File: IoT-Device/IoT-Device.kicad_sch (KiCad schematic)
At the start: 49 parts, among them J1 USB-C, J2 Conn_01x02, J3 SWD, SW1 RESET, SW2 BOOT_MODE, U1 BD33GA5WEFJ, U2 STM32U585VI, U3 BQ24074RGT, U4 ESP32-C3-WROOM-02

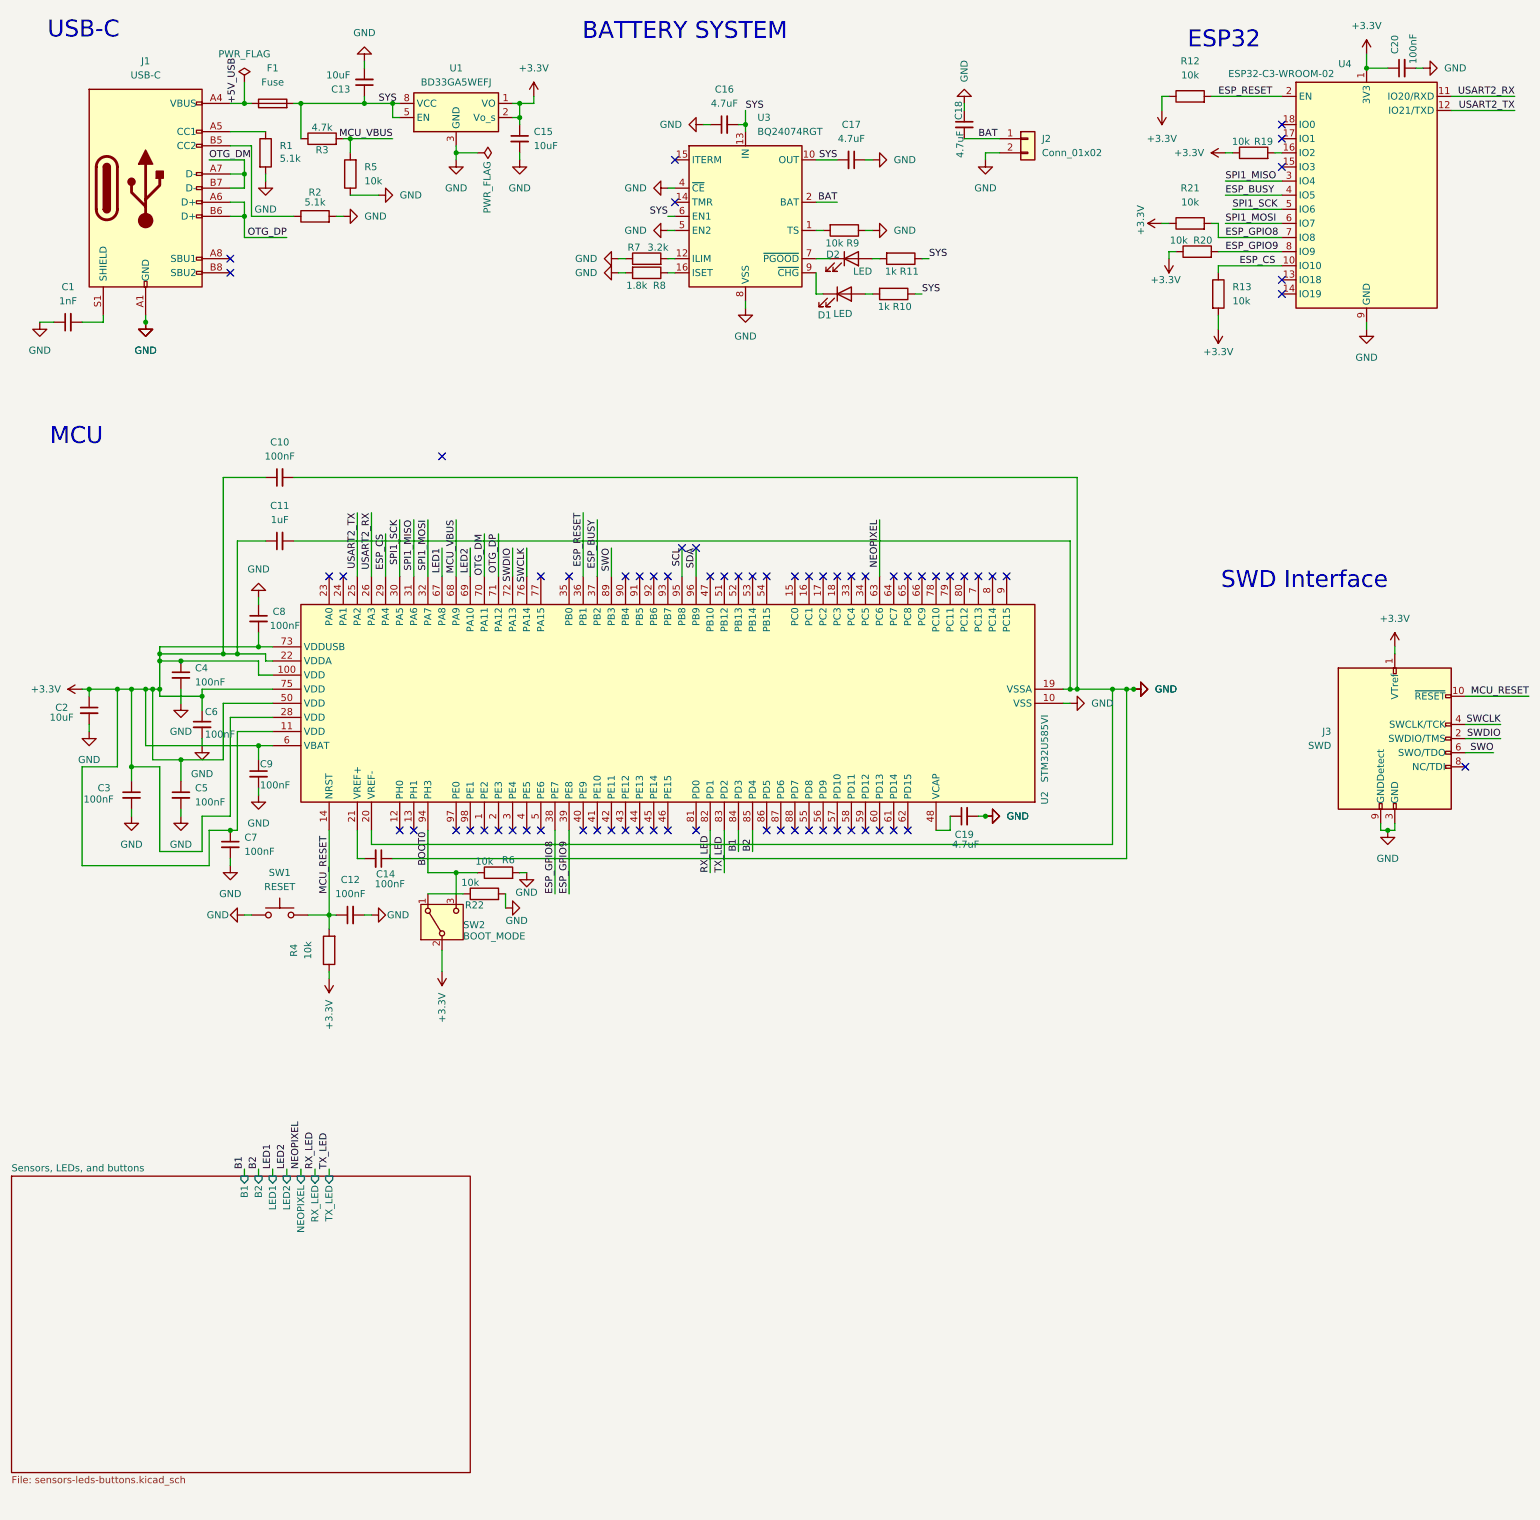
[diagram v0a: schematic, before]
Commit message: connect USB-C port's CC1 and CC2 to STM32's CC1 and CC2 pins
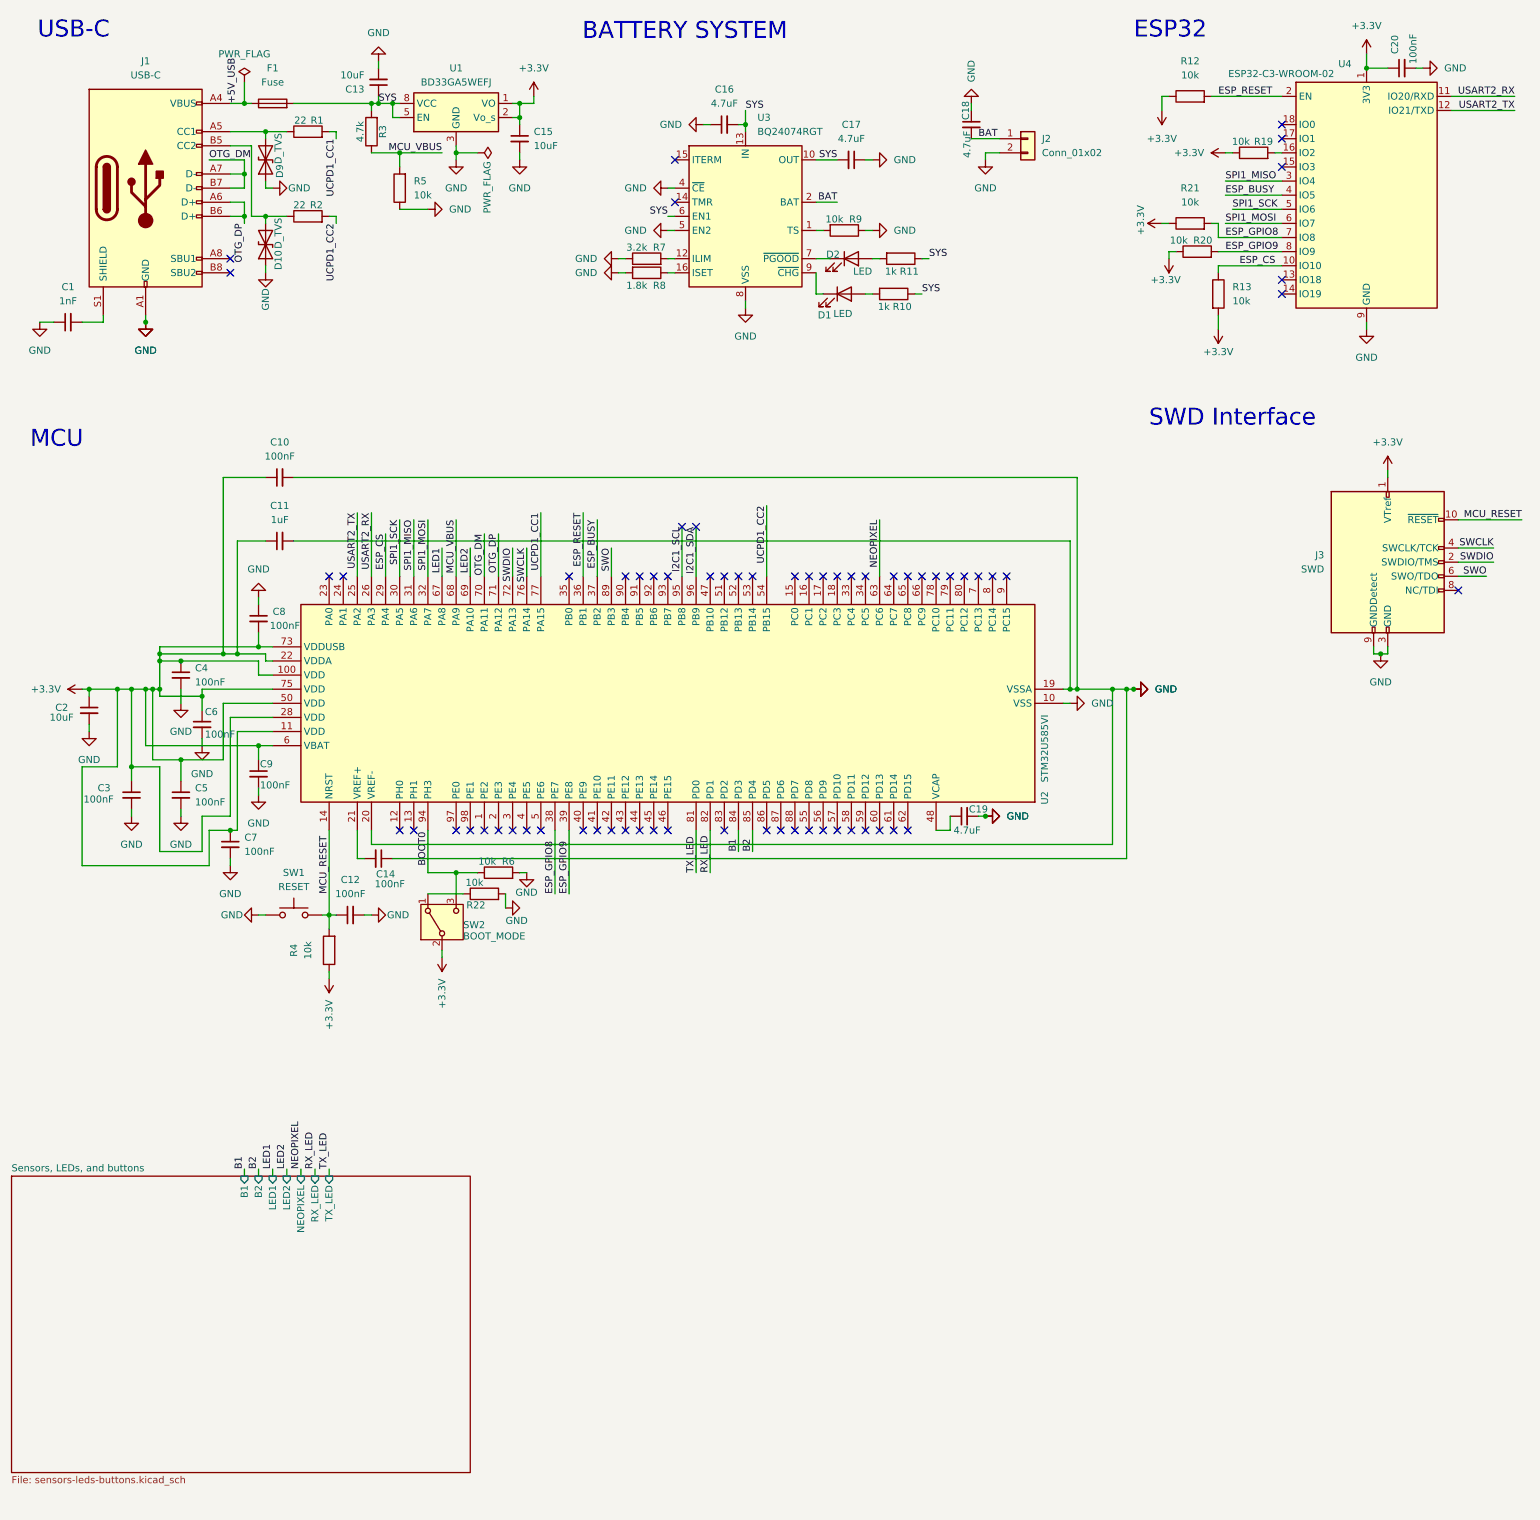
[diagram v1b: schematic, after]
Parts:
- added D10, D9: D_TVS, Diode_SMD:D_0603_1608Metric, symbol Device:D_TVS
- R1, R2: value 5.1k -> 22
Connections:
- net GND: now also D10.1 (A1), D9.1 (A1); no longer R1.2, R2.2
- net MCU_VBUS: now also R3.1; no longer R3.2
- net SYS: now also R3.2; no longer R3.1
- net TX_LED: now also U2.81 (PD0); no longer U2.83 (PD2)
- net at J1.B5 (CC2), R2.1: now also D10.2 (A2)
- net UCPD1_CC2: now reaches U2.54 (PB15)
- net UCPD1_CC2: now also R2.2
- net UCPD1_CC1: now reaches U2.77 (PA15)
- net UCPD1_CC1: now also R1.2
- net at J1.A5 (CC1), R1.1: now also D9.2 (A2)
- net SCL renamed I2C1_SCL
- net SDA renamed I2C1_SDA
- no-connect marks 69 -> 66
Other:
- moved on the sheet: C13, C18, J3, R1, R2, R3, R5, SW1

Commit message: add microSD card slot
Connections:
- net LED1: now also U2.57 (PD10); no longer U2.67 (PA8)
- net LED2: now also U2.58 (PD11); no longer U2.69 (PA10)
- net SD_DET_A: now reaches U2.55 (PD8)
- net SD_DET_B: now reaches U2.56 (PD9)
- net SDMMC1_D0: now reaches U2.65 (PC8)
- net SDMMC1_D1: now reaches U2.66 (PC9)
- net SDMMC1_D2: now reaches U2.78 (PC10)
- net SDMMC1_D3: now reaches U2.79 (PC11)
- net SDMMC1_CK: now reaches U2.80 (PC12)
- net SDMMC1_CMD: now reaches U2.83 (PD2)
- no-connect marks 66 -> 58
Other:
- added sheet Peripherals (peripherals.kicad_sch)
- note added: "Battery System"
- note removed: "BATTERY SYSTEM"

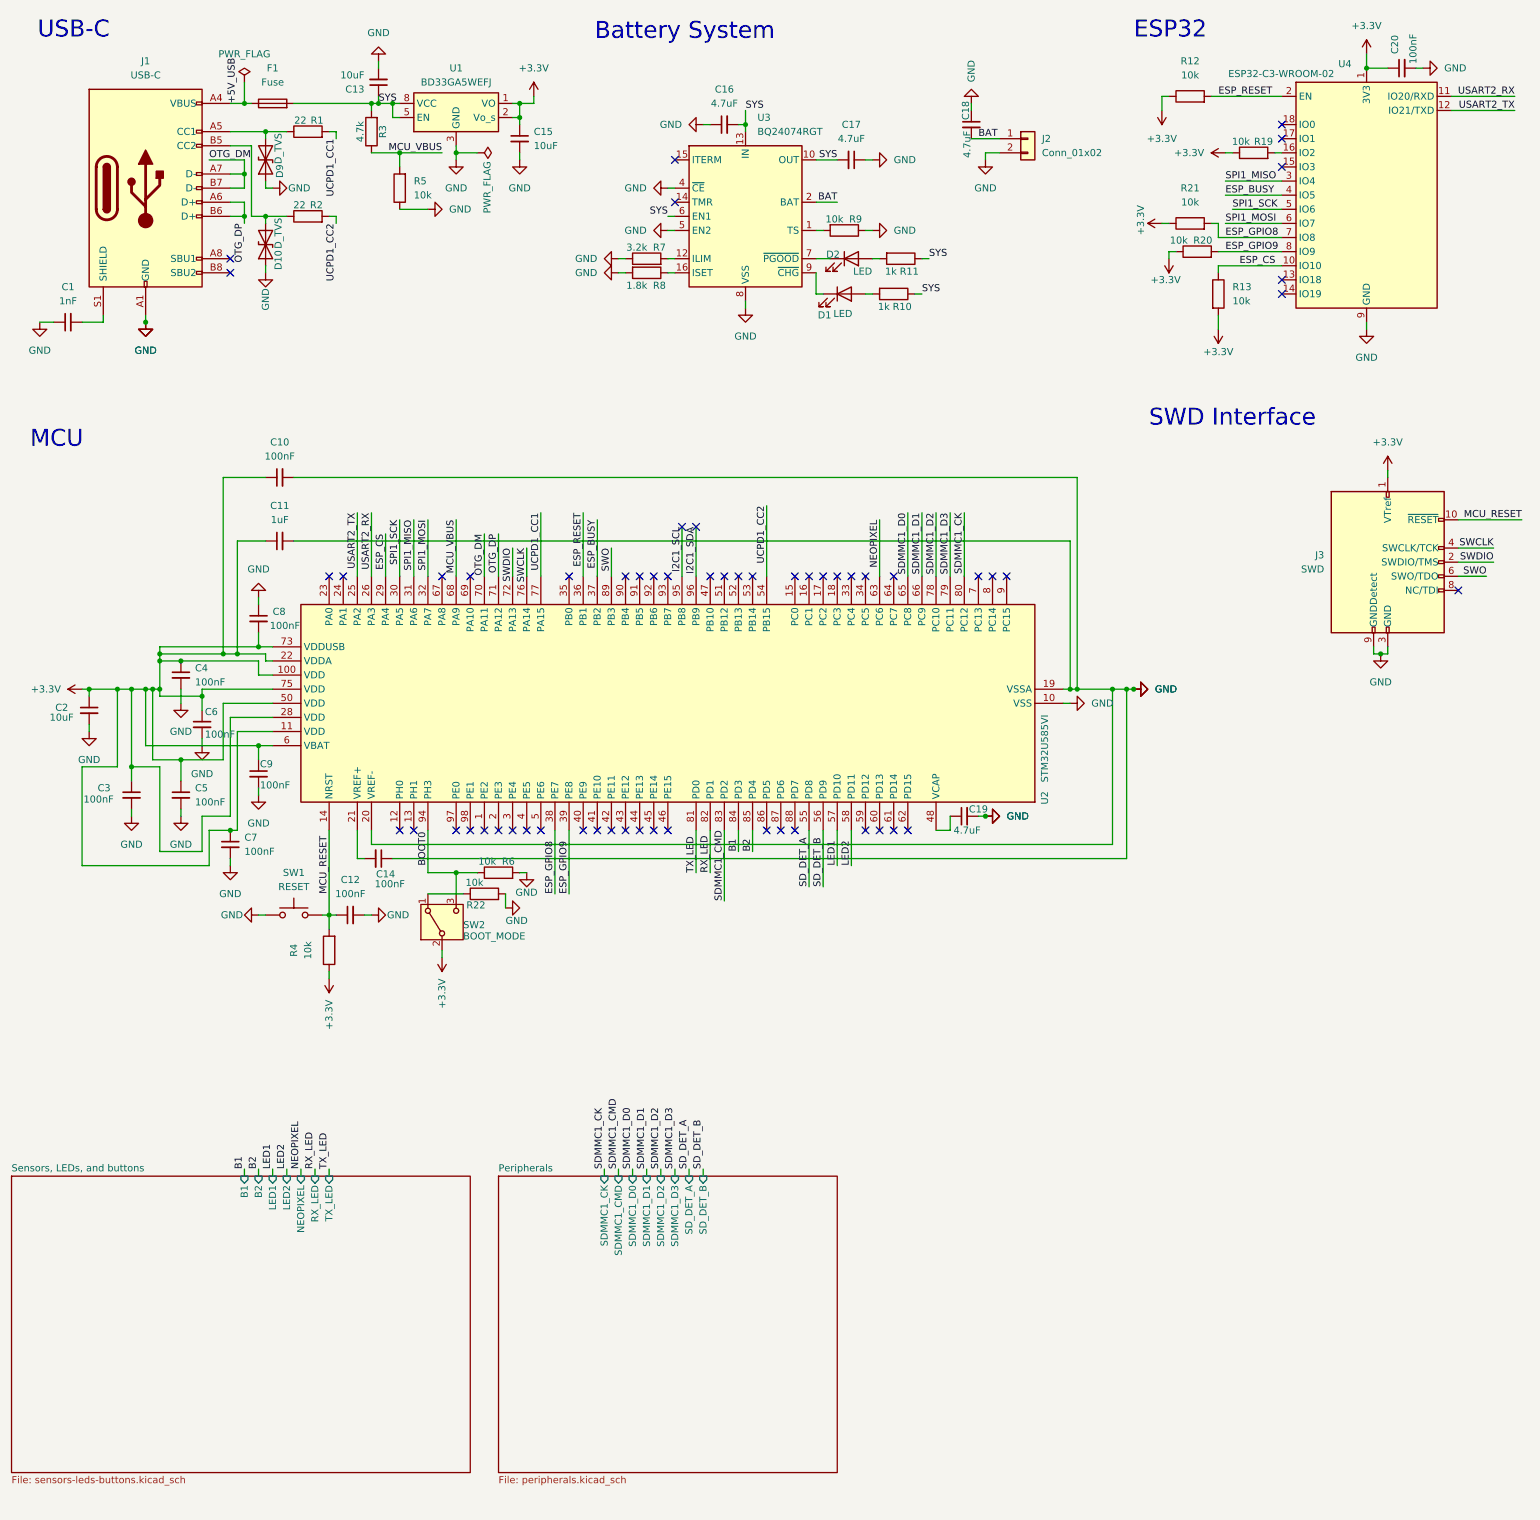
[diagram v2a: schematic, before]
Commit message: fix STM32<->ESP32-C3 UART communication, update labels on shcematics
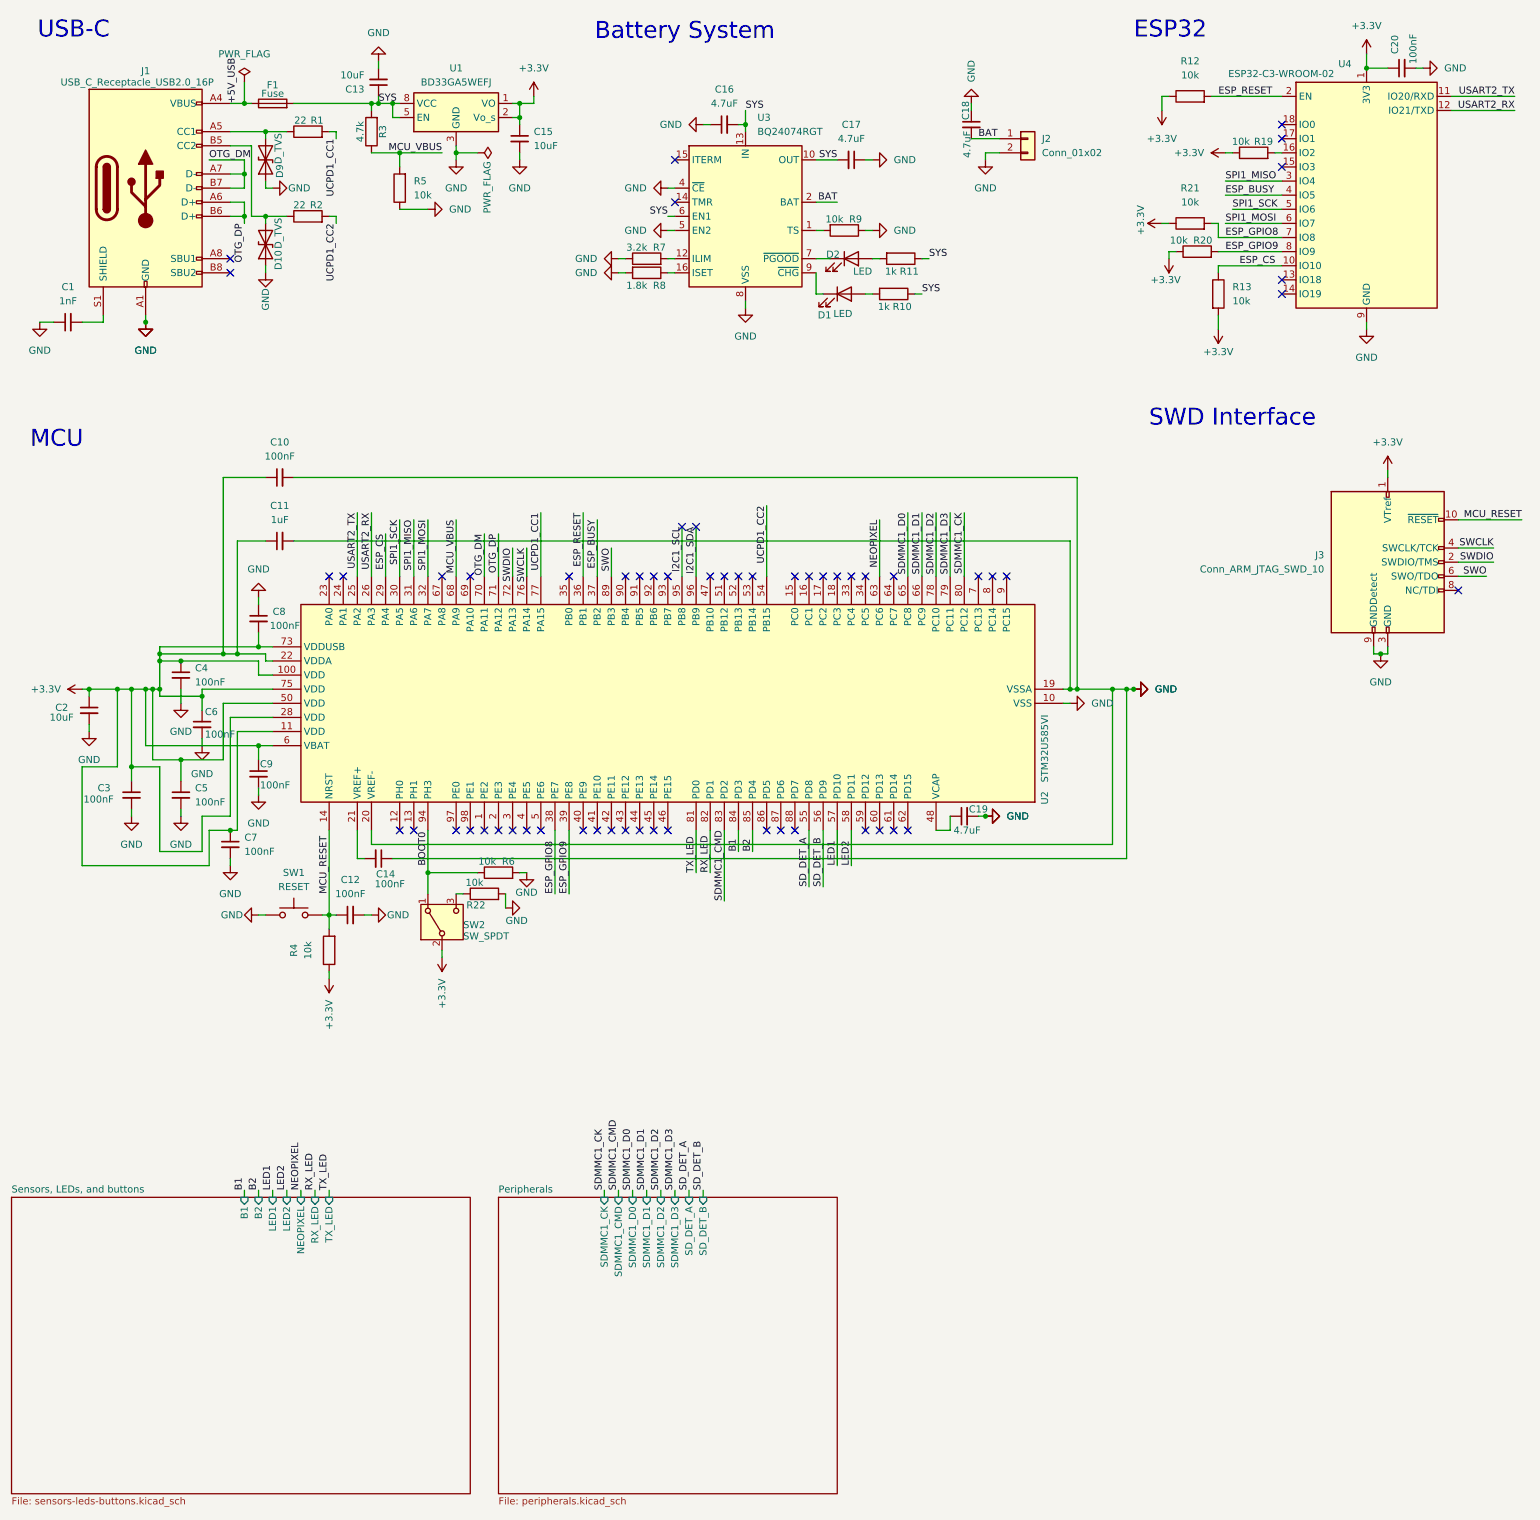
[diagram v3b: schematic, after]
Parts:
- J1: value USB-C -> USB_C_Receptacle_USB2.0_16P
- J3: value SWD -> Conn_ARM_JTAG_SWD_10
- SW2: value BOOT_MODE -> SW_SPDT
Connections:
- net BOOT0: now also SW2.1 (A); no longer SW2.3 (C)
- net USART2_RX: now also U4.12 (IO21/TXD); no longer U4.11 (IO20/RXD)
- net USART2_TX: now also U4.11 (IO20/RXD); no longer U4.12 (IO21/TXD)
- net at R22.1: now also SW2.3 (C); no longer SW2.1 (A)
